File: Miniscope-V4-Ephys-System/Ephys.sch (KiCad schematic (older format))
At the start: 18 parts, among them J1 34 Circuit Slimslack Connector, J23 Conn_01x01, J24 Conn_01x01, J25 Conn_01x01, J26 Conn_01x01, J27 Conn_01x01, J28 Conn_01x01, U1 RHD2132, U2 TXB0304RUT, U3 MCP1711T-30I/5X

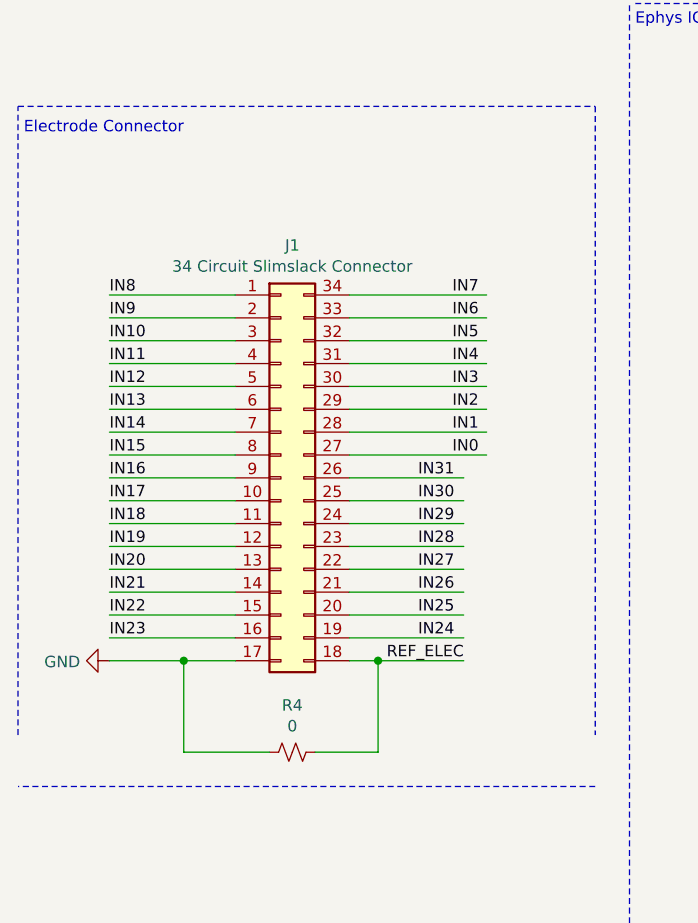
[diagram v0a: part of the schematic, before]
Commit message: Switch to female slimstack and reorder pins to batch 32ch silicon probe connector
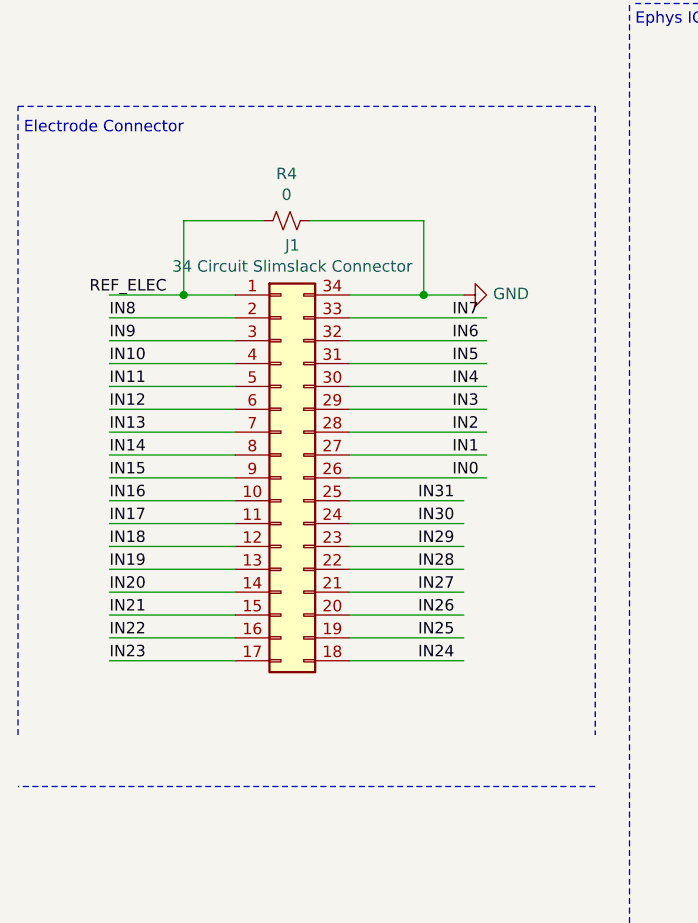
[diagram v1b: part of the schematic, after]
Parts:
- J1: footprint .Connector:SS_5046223412 -> .Connector:SS_5046183412
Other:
- moved on the sheet: R4
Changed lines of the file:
@@
 F 0 "J1" H 2000 4442 50  0000 C CNN
 F 1 "34  Circuit Slimslack Connector" H 2000 4350 50  0000 C CNN
-F 2 ".Connector:SS_5046223412" H 1950 3425 50  0001 C CNN
+F 2 ".Connector:SS_5046183412" H 1950 3425 50  0001 C CNN
 F 3 "~" H 1950 3425 50  0001 C CNN
 	1    1950 3425
@@
 	3325 4775 800  4775
 Wire Wire Line
+	1750 3925 1200 3925
+Wire Wire Line
+	1750 4025 1200 4025
+Wire Wire Line
+	1750 4125 1200 4125
+Wire Wire Line
+	1750 4225 1200 4225
+Text Label 1200 4225 0    50   ~ 0
+IN23
+Text Label 1200 4125 0    50   ~ 0
+IN22
+Text Label 1200 4025 0    50   ~ 0
+IN21
+Text Label 1200 3925 0    50   ~ 0
+IN20
+Text Label 1200 3825 0    50   ~ 0
+IN19
+Text Label 1200 3725 0    50   ~ 0
+IN18
+Text Label 1200 3625 0    50   ~ 0
+IN17
+Text Label 1200 3525 0    50   ~ 0
+IN16
+Text Label 1200 3425 0    50   ~ 0
+IN15
+Text Label 1200 3325 0    50   ~ 0
+IN14
+Text Label 1200 3225 0    50   ~ 0
+IN13
+Text Label 1200 3125 0    50   ~ 0
+IN12
+Text Label 1200 3025 0    50   ~ 0
+IN11
+Text Label 1200 2925 0    50   ~ 0
+IN10
+Text Label 1200 2825 0    50   ~ 0
+IN9
+Text Label 1200 2725 0    50   ~ 0
+IN8
+Wire Wire Line
 	1750 3825 1200 3825
 Wire Wire Line
-	1750 3925 1200 3925
-Wire Wire Line
-	1750 4025 1200 4025
-Wire Wire Line
-	1750 4125 1200 4125
-Text Label 1200 4125 0    50   ~ 0
-IN23
-Text Label 1200 4025 0    50   ~ 0
-IN22
-Text Label 1200 3925 0    50   ~ 0
-IN21
-Text Label 1200 3825 0    50   ~ 0
-IN20
-Text Label 1200 3725 0    50   ~ 0
-IN19
-Text Label 1200 3625 0    50   ~ 0
-IN18
-Text Label 1200 3525 0    50   ~ 0
-IN17
-Text Label 1200 3425 0    50   ~ 0
-IN16
-Text Label 1200 3325 0    50   ~ 0
-IN15
-Text Label 1200 3225 0    50   ~ 0
-IN14
-Text Label 1200 3125 0    50   ~ 0
-IN13
-Text Label 1200 3025 0    50   ~ 0
-IN12
-Text Label 1200 2925 0    50   ~ 0
-IN11
-Text Label 1200 2825 0    50   ~ 0
-IN10
-Text Label 1200 2725 0    50   ~ 0
-IN9
-Text Label 1200 2625 0    50   ~ 0
-IN8
-Wire Wire Line
 	1750 3725 1200 3725
 Wire Wire Line
@@
 	1750 2725 1200 2725
 Wire Wire Line
-	1750 2625 1200 2625
+	2250 3625 2750 3625
+Wire Wire Line
+	2250 3125 2850 3125
+Wire Wire Line
+	2250 3325 2850 3325
 Wire Wire Line
 	2250 3525 2750 3525
+Text Label 2550 4225 0    50   ~ 0
+IN24
+Text Label 2550 4125 0    50   ~ 0
+IN25
+Text Label 2550 4025 0    50   ~ 0
+IN26
+Text Label 2550 3925 0    50   ~ 0
+IN27
+Text Label 2550 3825 0    50   ~ 0
+IN28
+Text Label 2550 3725 0    50   ~ 0
+IN29
+Text Label 2550 3625 0    50   ~ 0
+IN30
+Text Label 2550 3525 0    50   ~ 0
+IN31
+Text Label 2700 3425 0    50   ~ 0
+IN0
+Text Label 2700 3325 0    50   ~ 0
+IN1
+Text Label 2700 3225 0    50   ~ 0
+IN2
+Text Label 2700 3125 0    50   ~ 0
+IN3
+Text Label 2700 3025 0    50   ~ 0
+IN4
+Text Label 2700 2925 0    50   ~ 0
+IN5
+Text Label 2700 2825 0    50   ~ 0
+IN6
+Wire Wire Line
+	2250 4225 2750 4225
+Wire Wire Line
+	2250 4125 2750 4125
+Wire Wire Line
+	2250 4025 2750 4025
+Wire Wire Line
+	2250 3925 2750 3925
+Wire Wire Line
+	2250 3825 2750 3825
+Wire Wire Line
+	2250 3725 2750 3725
+Wire Wire Line
+	2250 3425 2850 3425
+Wire Wire Line
+	2250 3225 2850 3225
 Wire Wire Line
 	2250 3025 2850 3025
 Wire Wire Line
-	2250 3225 2850 3225
-Wire Wire Line
-	2250 3425 2750 3425
-Text Label 2550 4125 0    50   ~ 0
-IN24
-Text Label 2550 4025 0    50   ~ 0
-IN25
-Text Label 2550 3925 0    50   ~ 0
-IN26
-Text Label 2550 3825 0    50   ~ 0
-IN27
-Text Label 2550 3725 0    50   ~ 0
-IN28
-Text Label 2550 3625 0    50   ~ 0
-IN29
-Text Label 2550 3525 0    50   ~ 0
-IN30
-Text Label 2550 3425 0    50   ~ 0
-IN31
-Text Label 2700 3325 0    50   ~ 0
-IN0
-Text Label 2700 3225 0    50   ~ 0
-IN1
-Text Label 2700 3125 0    50   ~ 0
-IN2
-Text Label 2700 3025 0    50   ~ 0
-IN3
-Text Label 2700 2925 0    50   ~ 0
-IN4
-Text Label 2700 2825 0    50   ~ 0
-IN5
+	2250 2925 2850 2925
+Wire Wire Line
+	2250 2825 2850 2825
 Text Label 2700 2725 0    50   ~ 0
-IN6
-Wire Wire Line
-	2250 4125 2750 4125
-Wire Wire Line
-	2250 4025 2750 4025
-Wire Wire Line
-	2250 3925 2750 3925
-Wire Wire Line
-	2250 3825 2750 3825
-Wire Wire Line
-	2250 3725 2750 3725
-Wire Wire Line
-	2250 3625 2750 3625
-Wire Wire Line
-	2250 3325 2850 3325
-Wire Wire Line
-	2250 3125 2850 3125
-Wire Wire Line
-	2250 2925 2850 2925
-Wire Wire Line
-	2250 2825 2850 2825
+IN7
 Wire Wire Line
 	2250 2725 2850 2725
-Text Label 2700 2625 0    50   ~ 0
-IN7
-Wire Wire Line
-	2250 2625 2850 2625
 $Comp
 L .Device:R_Small_US R?
 U 1 1 5EE9E203
-P 2000 4625
+P 1975 2300
 AR Path="/5EE9E203" Ref="R?"  Part="1"
 AR Path="/5EE85536/5EE9E203" Ref="R4"  Part="1"
-F 0 "R4" V 1795 4625 50  0000 C CNN
-F 1 "0" V 1886 4625 50  0000 C CNN
-F 2 ".Resistor:R_0201_0603Metric_ERJ_L" H 2000 4625 50  0001 C CNN
-F 3 "~" H 2000 4625 50  0001 C CNN
-	1    2000 4625
+F 0 "R4" V 1770 2300 50  0000 C CNN
+F 1 "0" V 1861 2300 50  0000 C CNN
+F 2 ".Resistor:R_0201_0603Metric_ERJ_L" H 1975 2300 50  0001 C CNN
+F 3 "~" H 1975 2300 50  0001 C CNN
+	1    1975 2300
 	0    1    1    0
 $EndComp
-Wire Wire Line
-	2375 4225 2750 4225
-Connection ~ 2375 4225
-Wire Wire Line
-	2375 4625 2375 4225
-Wire Wire Line
-	2100 4625 2375 4625
-Wire Wire Line
-	2250 4225 2375 4225
-Text Label 2750 4225 2    50   ~ 0
+Text Label 1450 2625 2    50   ~ 0
 REF_ELEC
-Wire Wire Line
-	1525 4225 1200 4225
-Connection ~ 1525 4225
-Wire Wire Line
-	1525 4625 1900 4625
-Wire Wire Line
-	1525 4225 1525 4625
-Wire Wire Line
-	1750 4225 1525 4225
 $Comp
 L power:GND #PWR?
 U 1 1 5EE9E214
-P 1200 4225
+P 2750 2625
 AR Path="/5EE9E214" Ref="#PWR?"  Part="1"
 AR Path="/5EE85536/5EE9E214" Ref="#PWR0101"  Part="1"
-F 0 "#PWR0101" H 1200 3975 50  0001 C CNN
-F 1 "GND" V 1205 4097 50  0000 R CNN
-F 2 "" H 1200 4225 50  0001 C CNN
-F 3 "" H 1200 4225 50  0001 C CNN
-	1    1200 4225
-	0    1    1    0
+F 0 "#PWR0101" H 2750 2375 50  0001 C CNN
+F 1 "GND" V 2755 2497 50  0000 R CNN
+F 2 "" H 2750 2625 50  0001 C CNN
+F 3 "" H 2750 2625 50  0001 C CNN
+	1    2750 2625
+	0    -1   -1   0
 $EndComp
 $Comp
@@
 Wire Wire Line
 	8575 5275 9325 5275
+Wire Wire Line
+	1200 2625 1525 2625
+Wire Wire Line
+	2250 2625 2575 2625
+Wire Wire Line
+	2575 2625 2575 2300
+Wire Wire Line
+	2575 2300 2075 2300
+Connection ~ 2575 2625
+Wire Wire Line
+	2575 2625 2750 2625
+Wire Wire Line
+	1875 2300 1525 2300
+Wire Wire Line
+	1525 2300 1525 2625
+Connection ~ 1525 2625
+Wire Wire Line
+	1525 2625 1750 2625
 $EndSCHEMATC

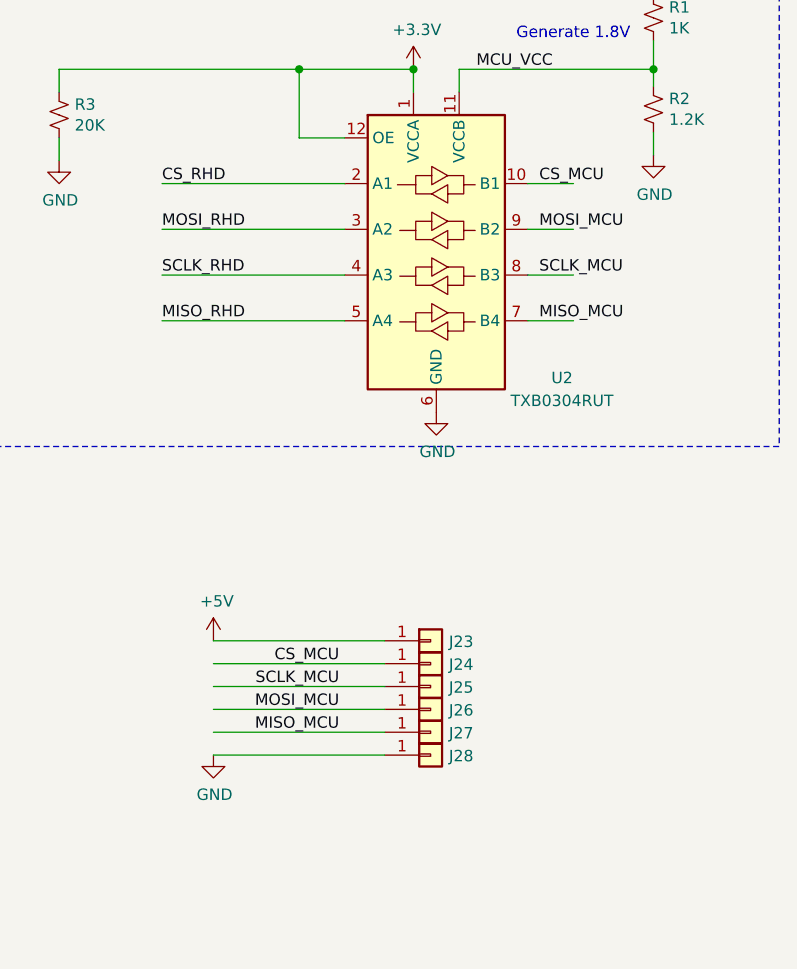
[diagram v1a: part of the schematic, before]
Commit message: Finish routing Ephys and Connector PCBs. Decrease layer count to 4.
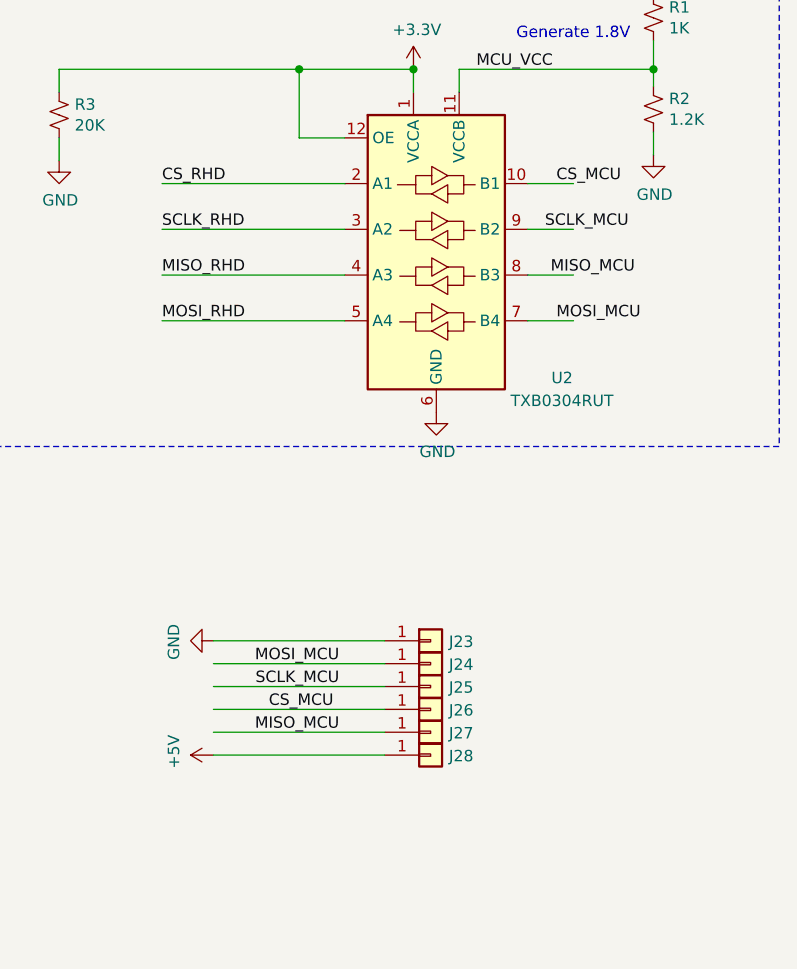
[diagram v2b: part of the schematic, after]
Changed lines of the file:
@@
 	1    0    0    -1
 $EndComp
+Text Label 8350 3675 0    50   ~ 0
+MISO_RHD
+Wire Wire Line
+	9150 3875 8350 3875
+Text Label 8350 3475 0    50   ~ 0
+SCLK_RHD
 Text Label 8350 3875 0    50   ~ 0
-MISO_RHD
-Wire Wire Line
-	9150 3875 8350 3875
-Text Label 8350 3675 0    50   ~ 0
-SCLK_RHD
-Text Label 8350 3475 0    50   ~ 0
 MOSI_RHD
 Text Label 8350 3275 0    50   ~ 0
@@
 Text Notes 1000 5875 0    50   ~ 0
 +3.3V Regulator
-Text Label 10000 3275 0    50   ~ 0
+Text Label 10075 3275 0    50   ~ 0
 CS_MCU
-Text Label 10000 3475 0    50   ~ 0
+Text Label 10075 3875 0    50   ~ 0
 MOSI_MCU
-Text Label 10000 3675 0    50   ~ 0
+Text Label 10025 3475 0    50   ~ 0
 SCLK_MCU
-Text Label 10000 3875 0    50   ~ 0
+Text Label 10050 3675 0    50   ~ 0
 MISO_MCU
 $Comp
 L power:+5V #PWR?
 U 1 1 5F13ABB9
-P 8575 5275
+P 8575 5775
 AR Path="/5EEA60FC/5F13ABB9" Ref="#PWR?"  Part="1"
 AR Path="/5EEA5765/5F13ABB9" Ref="#PWR?"  Part="1"
 AR Path="/5EE85536/5F13ABB9" Ref="#PWR01"  Part="1"
-F 0 "#PWR01" H 8575 5125 50  0001 C CNN
-F 1 "+5V" H 8590 5448 50  0000 C CNN
+F 0 "#PWR01" H 8575 5625 50  0001 C CNN
+F 1 "+5V" H 8590 5948 50  0000 C CNN
+F 2 "" H 8575 5775 50  0001 C CNN
+F 3 "" H 8575 5775 50  0001 C CNN
+	1    8575 5775
+	0    -1   -1   0
+$EndComp
+$Comp
+L power:GND #PWR?
+U 1 1 5F13ABBF
+P 8575 5275
+AR Path="/5EEA60FC/5F13ABBF" Ref="#PWR?"  Part="1"
+AR Path="/5EEA5765/5F13ABBF" Ref="#PWR?"  Part="1"
+AR Path="/5EE85536/5F13ABBF" Ref="#PWR02"  Part="1"
+F 0 "#PWR02" H 8575 5025 50  0001 C CNN
+F 1 "GND" H 8580 5102 50  0000 C CNN
 F 2 "" H 8575 5275 50  0001 C CNN
 F 3 "" H 8575 5275 50  0001 C CNN
 	1    8575 5275
-	1    0    0    -1
-$EndComp
-$Comp
-L power:GND #PWR?
-U 1 1 5F13ABBF
-P 8575 5775
-AR Path="/5EEA60FC/5F13ABBF" Ref="#PWR?"  Part="1"
-AR Path="/5EEA5765/5F13ABBF" Ref="#PWR?"  Part="1"
-AR Path="/5EE85536/5F13ABBF" Ref="#PWR02"  Part="1"
-F 0 "#PWR02" H 8575 5525 50  0001 C CNN
-F 1 "GND" H 8580 5602 50  0000 C CNN
-F 2 "" H 8575 5775 50  0001 C CNN
-F 3 "" H 8575 5775 50  0001 C CNN
-	1    8575 5775
-	1    0    0    -1
+	0    1    1    0
 $EndComp
 Text Label 9125 5675 2    50   ~ 0
 MISO_MCU
-Text Label 9125 5575 2    50   ~ 0
+Text Label 9125 5375 2    50   ~ 0
 MOSI_MCU
 Text Label 9125 5475 2    50   ~ 0
 SCLK_MCU
-Text Label 9125 5375 2    50   ~ 0
+Text Label 9100 5575 2    50   ~ 0
 CS_MCU
 $Comp
